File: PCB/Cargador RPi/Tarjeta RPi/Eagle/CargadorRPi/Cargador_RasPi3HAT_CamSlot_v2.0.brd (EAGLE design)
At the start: 65 x 56 mm, 26 parts, among them J2 PIN20X2, U1 MCP3208, X1 ZX62D-B-5PA8

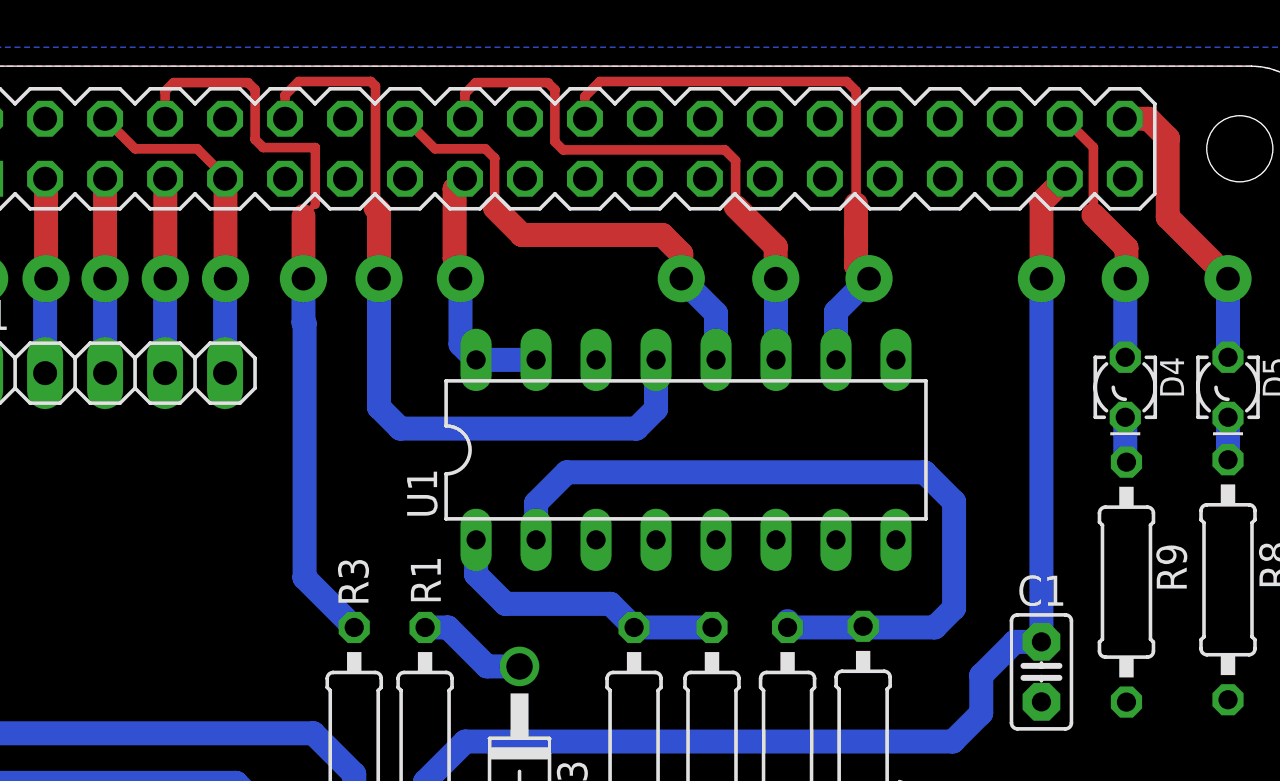
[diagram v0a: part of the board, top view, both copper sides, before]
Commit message: Se mejoran algunas pistas del PCB
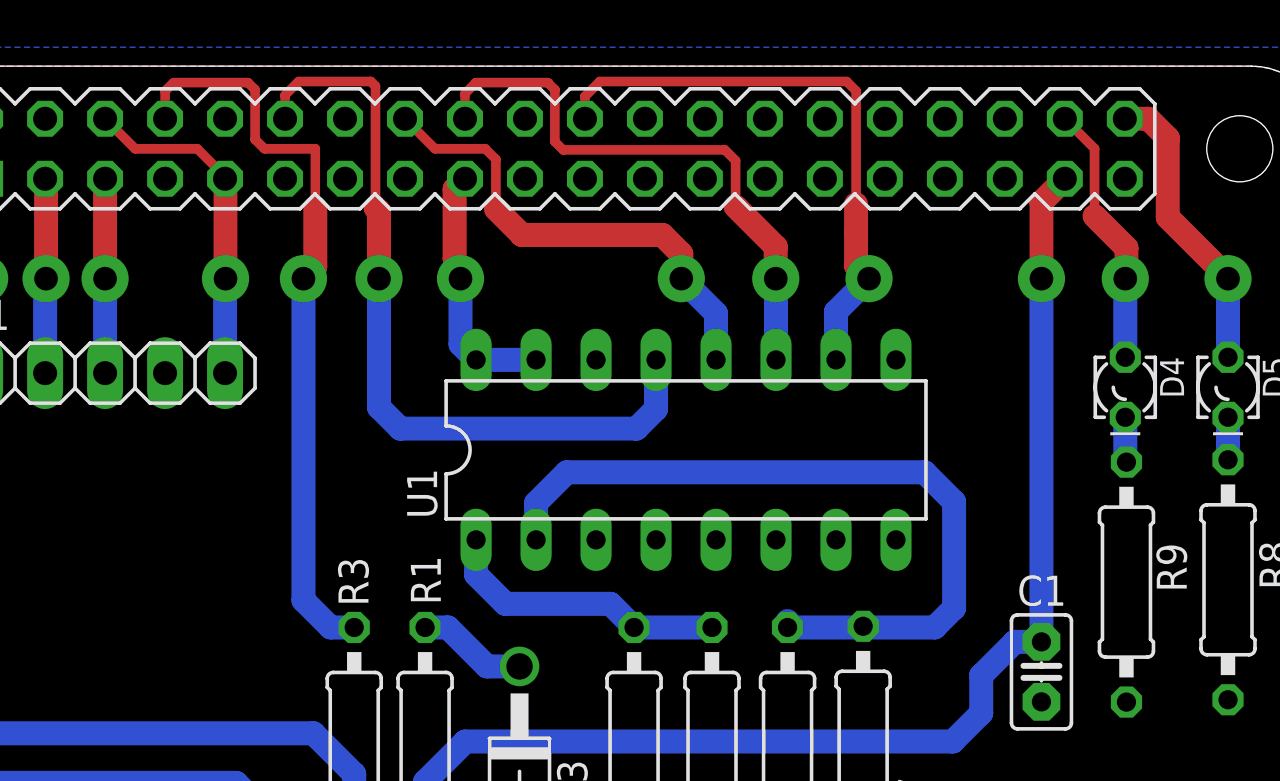
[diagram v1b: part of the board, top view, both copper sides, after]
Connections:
- removed net NC: J2.7, JP1.4
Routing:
- net NC: track 8.23 -> 0.00 mm, vias 1 -> 0
- net N$17: track 31.5 -> 32.0 mm
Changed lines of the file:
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@@
 <drawing>
 <settings>
-<setting alwaysvectorfont="no"/>
+<setting alwaysvectorfont="yes"/>
 <setting keepoldvectorfont="yes"/>
 <setting verticaltext="up"/>
@@
 <wire x1="16.35" y1="55.3" x2="19.5" y2="55.3" width="0.4064" layer="1"/>
 <wire x1="19.8" y1="55" x2="19.8" y2="52.9" width="0.4064" layer="1"/>
-<wire x1="19.8" y1="52.9" x2="20.15" y2="52.55" width="0.4064" layer="1"/>
-<wire x1="20.15" y1="52.55" x2="22.35" y2="52.55" width="0.4064" layer="1"/>
+<wire x1="19.8" y1="52.9" x2="20.2" y2="52.5" width="0.4064" layer="1"/>
+<wire x1="20.2" y1="52.5" x2="22.35" y2="52.5" width="0.4064" layer="1"/>
 <wire x1="19.5" y1="55.3" x2="19.8" y2="55" width="0.4064" layer="1"/>
-<wire x1="22.35" y1="50.15" x2="22.35" y2="52.55" width="0.4064" layer="1"/>
+<wire x1="22.35" y1="50" x2="22.35" y2="52.5" width="0.4064" layer="1"/>
 <contactref element="R3" pad="2"/>
-<wire x1="21.9" y1="45.100003125" x2="21.85" y2="45.150003125" width="1.016" layer="16"/>
-<wire x1="21.9" y1="45.100003125" x2="21.9" y2="34.38" width="1.016" layer="16"/>
-<wire x1="21.9" y1="34.38" x2="21.893" y2="34.337" width="1.016" layer="16"/>
-<wire x1="24" y1="32.23" x2="21.893" y2="34.337" width="1.016" layer="16"/>
-<wire x1="21.85" y1="45.150003125" x2="21.85" y2="47" width="1.016" layer="16"/>
+<wire x1="21.85" y1="47" x2="21.85" y2="33.38" width="1.016" layer="16"/>
+<wire x1="24" y1="32.23" x2="23" y2="32.23" width="1.016" layer="16"/>
+<wire x1="23" y1="32.23" x2="21.85" y2="33.38" width="1.016" layer="16"/>
 <via x="21.85" y="47" extent="1-16" drill="1" diameter="2" shape="octagon"/>
-<wire x1="21.85" y1="49.65" x2="22.35" y2="50.15" width="0.254" layer="1"/>
-<wire x1="21.85" y1="47" x2="21.85" y2="49.65" width="1.016" layer="1"/>
+<wire x1="22.35" y1="50" x2="22.35" y2="47.5" width="1.016" layer="1"/>
+<wire x1="21.85" y1="47" x2="22.35" y2="47.5" width="1.016" layer="1"/>
 </signal>
 <signal name="N$18">
@@
 <wire x1="26.15" y1="53.77" x2="27.42" y2="52.5" width="0.4064" layer="1"/>
 <wire x1="27.42" y1="52.5" x2="29.55" y2="52.5" width="0.4064" layer="1"/>
-<wire x1="29.55" y1="52.5" x2="29.95" y2="52.1" width="0.4064" layer="1"/>
-<wire x1="29.95" y1="52.1" x2="29.95" y2="50" width="0.4064" layer="1"/>
-<wire x1="29.95" y1="50" x2="31.1" y2="48.85" width="1.016" layer="1"/>
+<wire x1="29.55" y1="52.5" x2="30" y2="52.05" width="0.4064" layer="1"/>
+<wire x1="30" y1="52.05" x2="30" y2="49.95" width="0.4064" layer="1"/>
+<wire x1="30" y1="49.95" x2="31.1" y2="48.85" width="1.016" layer="1"/>
 <wire x1="31.1" y1="48.85" x2="37.05" y2="48.85" width="1.016" layer="1"/>
 <wire x1="37.05" y1="48.85" x2="37.85" y2="48.05" width="1.016" layer="1"/>
@@
 <signal name="N$7">
 <contactref element="J2" pad="38"/>
-<wire x1="54.09" y1="53.77" x2="55.3" y2="52.56" width="0.4064" layer="1"/>
-<wire x1="55.3" y1="52.56" x2="55.3" y2="49.7" width="0.4064" layer="1"/>
-<wire x1="56.7" y1="48.3" x2="55.3" y2="49.7" width="1.016" layer="1"/>
+<wire x1="54.09" y1="53.77" x2="55.35" y2="52.51" width="0.4064" layer="1"/>
+<wire x1="55.35" y1="52.51" x2="55.35" y2="49.65" width="0.4064" layer="1"/>
+<wire x1="56.7" y1="48.3" x2="55.35" y2="49.65" width="1.016" layer="1"/>
 <contactref element="D4" pad="A"/>
 <wire x1="56.65" y1="43.67" x2="56.65" y2="47" width="1.016" layer="16"/>
@@
 <wire x1="13.45" y1="47" x2="13.45" y2="43" width="1.016" layer="16"/>
 </signal>
-<signal name="NC">
-<contactref element="JP1" pad="4"/>
-<contactref element="J2" pad="7"/>
-<wire x1="15.99" y1="43" x2="15.99" y2="46.89" width="1.016" layer="16"/>
-<wire x1="15.99" y1="46.89" x2="16" y2="47" width="0.1524" layer="16"/>
-<via x="16" y="47" extent="1-16" drill="1" diameter="2" shape="octagon"/>
-<wire x1="16" y1="47" x2="16" y2="51.22" width="1.016" layer="1"/>
-<wire x1="16" y1="51.22" x2="15.99" y2="51.23" width="0.1524" layer="1"/>
-</signal>
 <signal name="N$1">
